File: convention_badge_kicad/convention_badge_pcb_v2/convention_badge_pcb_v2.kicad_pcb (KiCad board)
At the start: 4 copper layers, 90 x 98 mm, 56 parts, among them J1 USBC, J2 Conn_01x03_Pin, J3 3.7V Battery, J4 Conn_01x07_Pin, J5 Conn_01x07_Pin, Q1 AO3401A, SW1 SW4X2, SW2 SW4X2, SW3 SW_Push, SW4 SW_Push, SW5 SW_Push, SW6 SW4X2, U1 ESP32-C3-WROOM-02, U2 FS8205A, U3 TP4056, U4 DW01A, U5 TLV75733PDBV

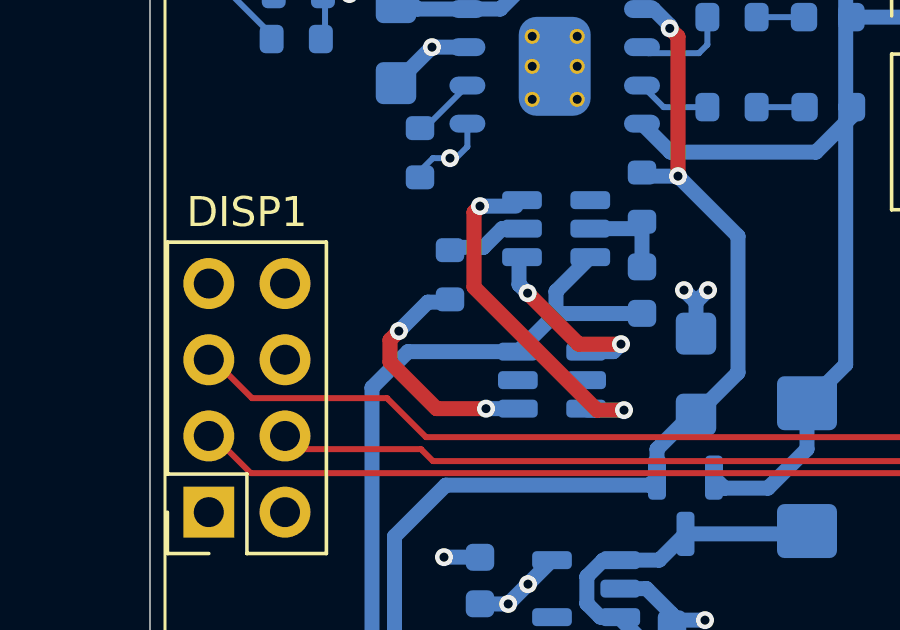
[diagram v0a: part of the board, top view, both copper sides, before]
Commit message: add readme content, modify pins in code for C3
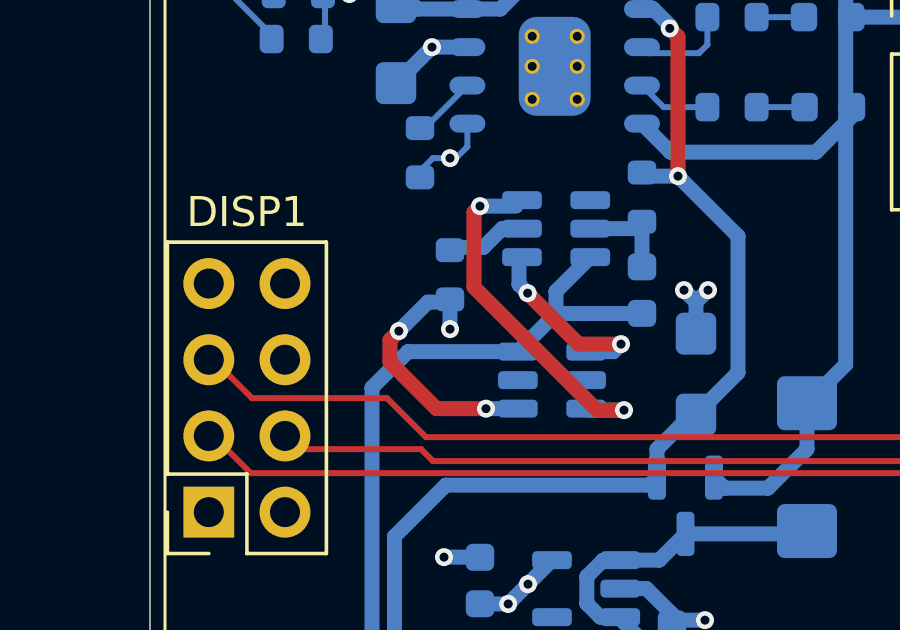
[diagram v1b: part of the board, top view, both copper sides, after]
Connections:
- R9 pad 1: Net-(U2-S1) -> GND
- U2 pad 1: Net-(U2-S1) -> GND
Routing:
- net GND: track 65.1 -> 74.3 mm, vias 23 -> 26
- net Net-(U2-S1): track 8.17 -> 0.00 mm, vias 2 -> 0
